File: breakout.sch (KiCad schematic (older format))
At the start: 32 parts, among them CON1 SD_Card, CON2 USB-MICRO-AB, P2 CONN_01X40, P3 CONN_01X40, P4 CONN_01X40, P5 A-DF-09-A/KG-T4S, SW1 SW_PUSH

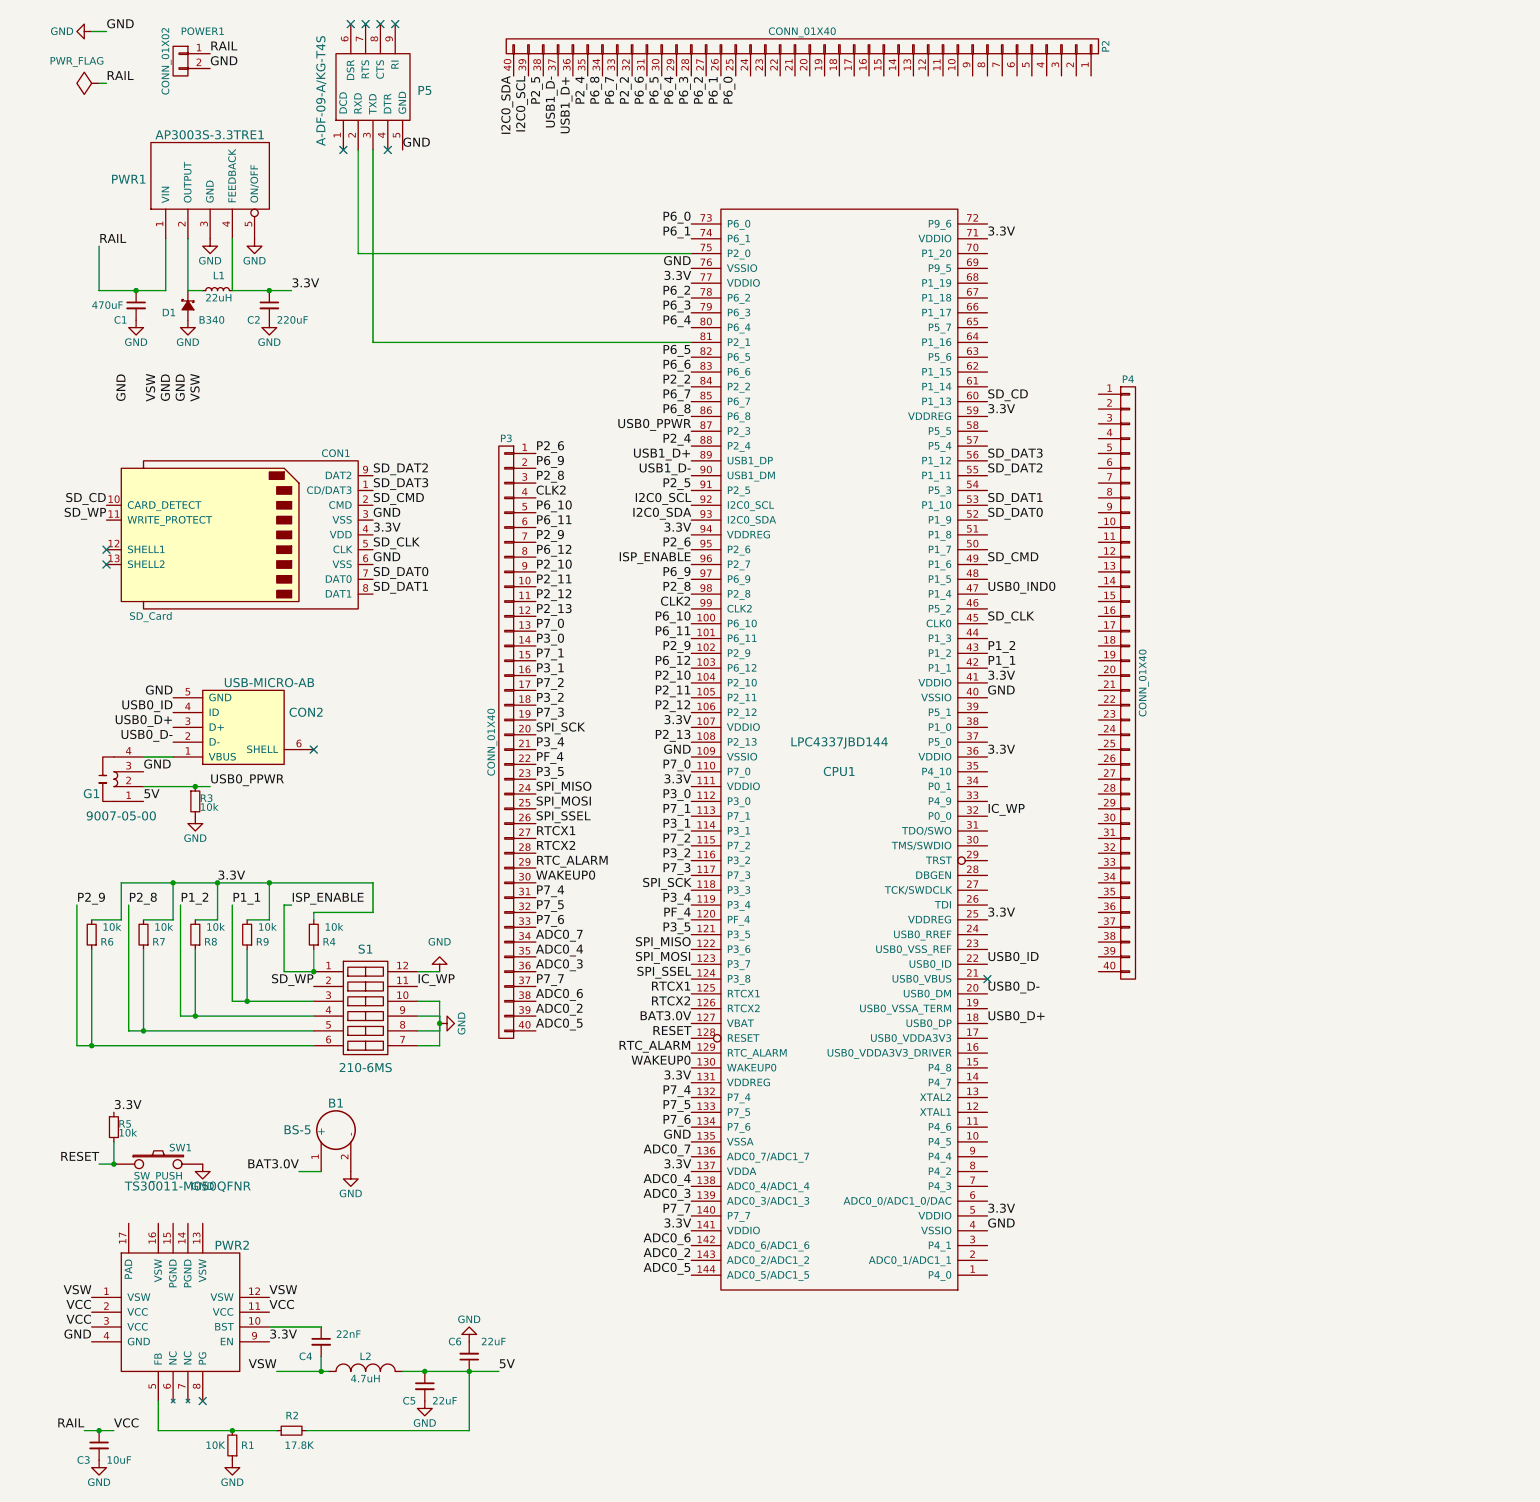
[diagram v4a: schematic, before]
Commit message: fully netlisted CPU1
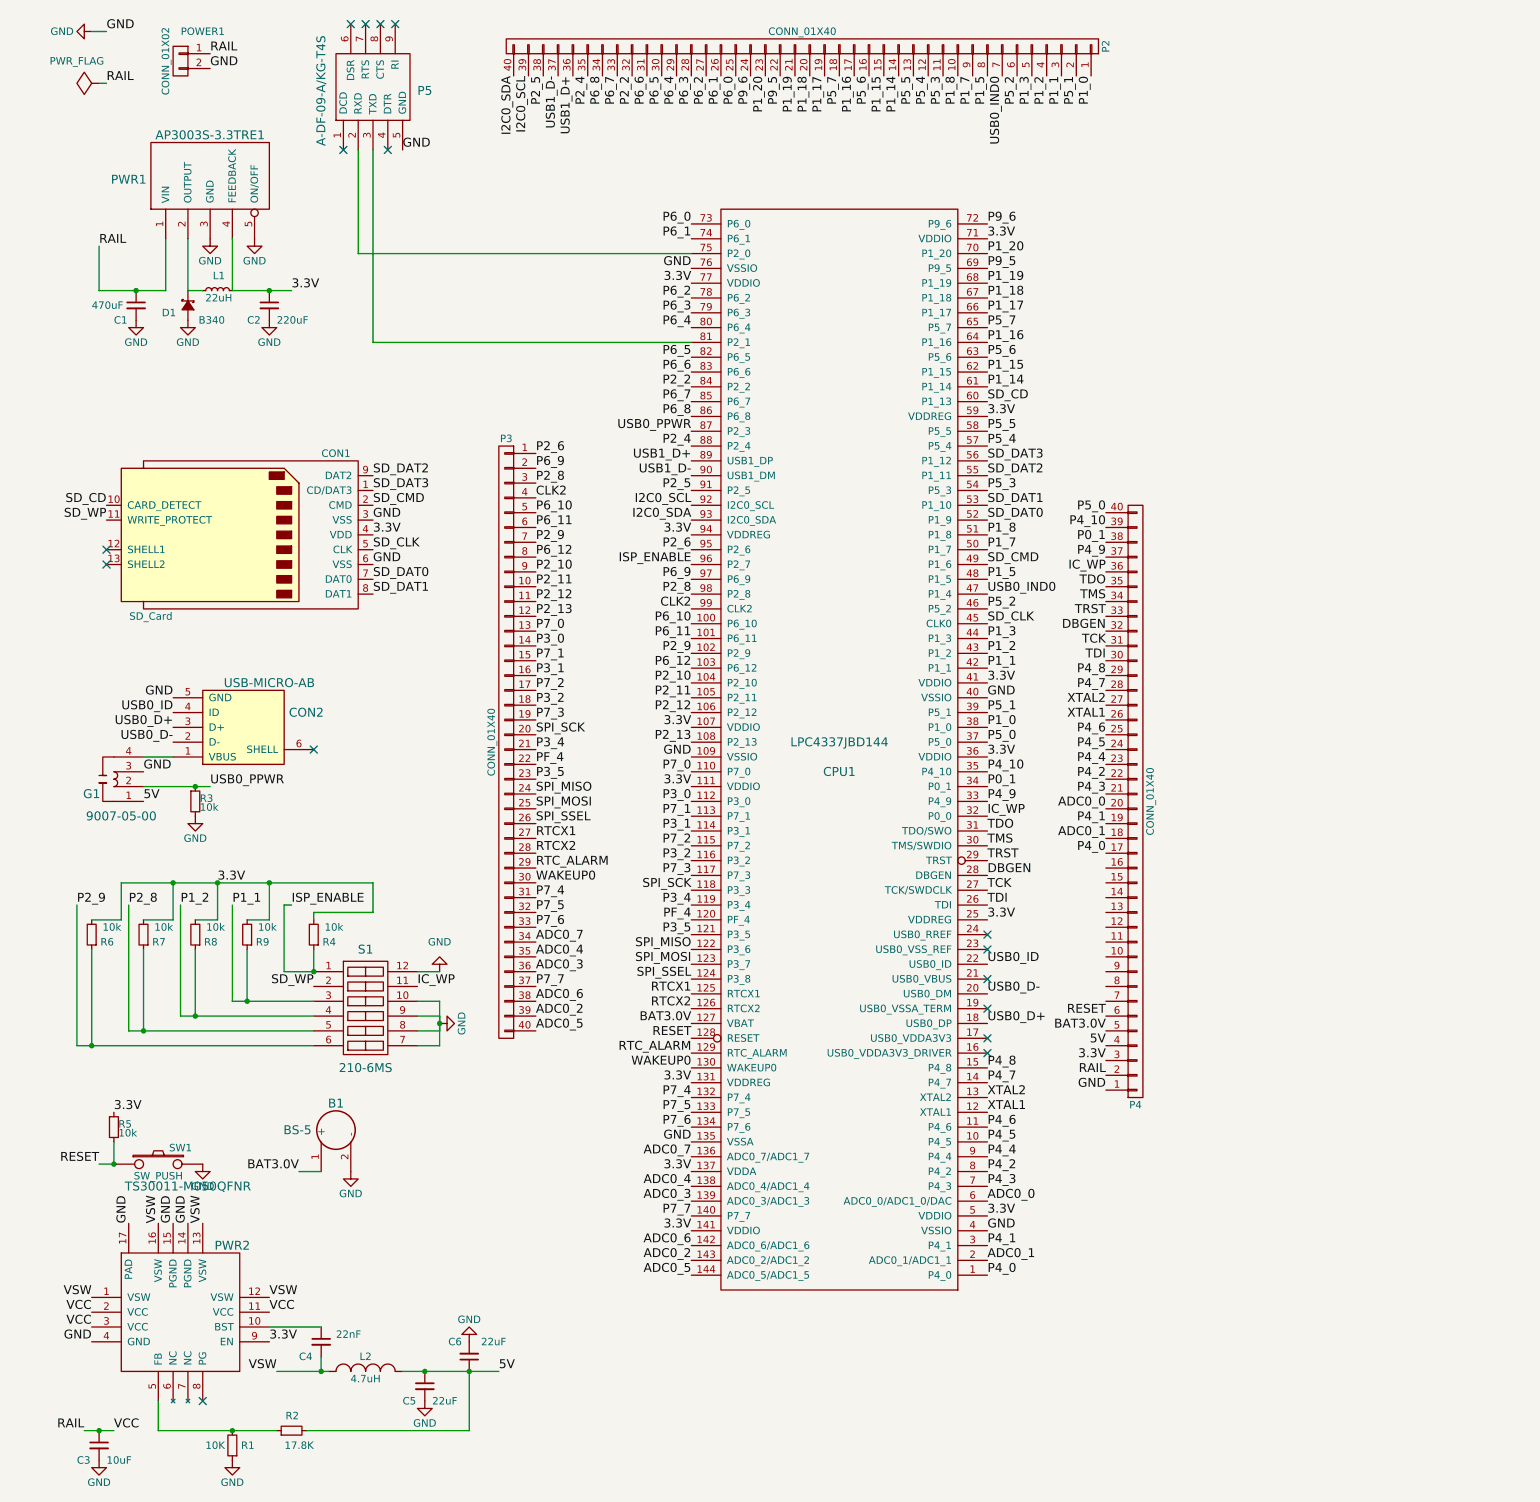
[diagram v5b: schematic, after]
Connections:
- net 3.3V: now also P4.3 (P3)
- net 5V: now also P4.4 (P4)
- net BAT3.0V: now also P4.5 (P5)
- net GND: now also P4.1 (P1), PWR2.14 (PGND), PWR2.15 (PGND), PWR2.17 (PAD)
- net IC_WP: now also P4.36 (P36)
- net P1_1: now also P2.3 (P3)
- net P1_2: now also P2.4 (P4)
- net RAIL: now also P4.2 (P2)
- net RESET: now also P4.6 (P6)
- net USB0_IND0: now also P2.7 (P7)
- net VSW: now also PWR2.13 (VSW), PWR2.16 (VSW)
- net P4_0: now reaches CPU1.1 (P4_0)
- net P4_0: now also P4.17 (P17)
- net P4_5: now reaches CPU1.10 (P4_5)
- net P4_5: now also P4.24 (P24)
- net P4_6: now reaches CPU1.11 (P4_6)
- net P4_6: now also P4.25 (P25)
- net XTAL1: now reaches CPU1.12 (XTAL1)
- net XTAL1: now also P4.26 (P26)
- net XTAL2: now reaches CPU1.13 (XTAL2)
- net XTAL2: now also P4.27 (P27)
- net P4_7: now reaches CPU1.14 (P4_7)
- net P4_7: now also P4.28 (P28)
- net P4_8: now reaches CPU1.15 (P4_8)
- net P4_8: now also P4.29 (P29)
- net ADC0_1: now reaches CPU1.2 (ADC0_1/ADC1_1)
- net ADC0_1: now also P4.18 (P18)
- net TDI: now reaches CPU1.26 (TDI)
- net TDI: now also P4.30 (P30)
- net TCK: now reaches CPU1.27 (TCK/SWDCLK)
- net TCK: now also P4.31 (P31)
- net DBGEN: now reaches CPU1.28 (DBGEN)
- net DBGEN: now also P4.32 (P32)
- net TRST: now reaches CPU1.29 (TRST)
- net TRST: now also P4.33 (P33)
- net P4_1: now reaches CPU1.3 (P4_1)
- net P4_1: now also P4.19 (P19)
- net TMS: now reaches CPU1.30 (TMS/SWDIO)
- net TMS: now also P4.34 (P34)
- net TDO: now reaches CPU1.31 (TDO/SWO)
- net TDO: now also P4.35 (P35)
- net P4_9: now reaches CPU1.33 (P4_9)
- net P4_9: now also P4.37 (P37)
- net P0_1: now reaches CPU1.34 (P0_1)
- net P0_1: now also P4.38 (P38)
- net P4_10: now reaches CPU1.35 (P4_10)
- net P4_10: now also P4.39 (P39)
- net P5_0: now reaches CPU1.37 (P5_0)
- net P5_0: now also P4.40 (P40)
- net P1_0: now reaches CPU1.38 (P1_0)
- net P1_0: now also P2.1 (P1)
- net P5_1: now reaches CPU1.39 (P5_1)
- net P5_1: now also P2.2 (P2)
- net P1_3: now reaches CPU1.44 (P1_3)
- net P1_3: now also P2.5 (P5)
- net P5_2: now reaches CPU1.46 (P5_2)
- net P5_2: now also P2.6 (P6)
- net P1_5: now reaches CPU1.48 (P1_5)
- net P1_5: now also P2.8 (P8)
- net P1_7: now reaches CPU1.50 (P1_7)
- net P1_7: now also P2.9 (P9)
- net P1_8: now reaches CPU1.51 (P1_8)
- net P1_8: now also P2.10 (P10)
- net P5_3: now reaches CPU1.54 (P5_3)
- net P5_3: now also P2.11 (P11)
- net P5_4: now reaches CPU1.57 (P5_4)
- net P5_4: now also P2.12 (P12)
- net P5_5: now reaches CPU1.58 (P5_5)
- net P5_5: now also P2.13 (P13)
- net ADC0_0: now reaches CPU1.6 (ADC0_0/ADC1_0/DAC)
- net ADC0_0: now also P4.20 (P20)
- net P1_14: now reaches CPU1.61 (P1_14)
- net P1_14: now also P2.14 (P14)
- net P1_15: now reaches CPU1.62 (P1_15)
- net P1_15: now also P2.15 (P15)
- net P5_6: now reaches CPU1.63 (P5_6)
- net P5_6: now also P2.16 (P16)
- net P1_16: now reaches CPU1.64 (P1_16)
- net P1_16: now also P2.17 (P17)
- net P5_7: now reaches CPU1.65 (P5_7)
- net P5_7: now also P2.18 (P18)
- net P1_17: now reaches CPU1.66 (P1_17)
- net P1_17: now also P2.19 (P19)
- net P1_18: now reaches CPU1.67 (P1_18)
- net P1_18: now also P2.20 (P20)
- net P1_19: now reaches CPU1.68 (P1_19)
- net P1_19: now also P2.21 (P21)
- net P9_5: now reaches CPU1.69 (P9_5)
- net P9_5: now also P2.22 (P22)
- net P4_3: now reaches CPU1.7 (P4_3)
- net P4_3: now also P4.21 (P21)
- net P1_20: now reaches CPU1.70 (P1_20)
- net P1_20: now also P2.23 (P23)
- net P9_6: now reaches CPU1.72 (P9_6)
- net P9_6: now also P2.24 (P24)
- net P4_2: now reaches CPU1.8 (P4_2)
- net P4_2: now also P4.22 (P22)
- net P4_4: now reaches CPU1.9 (P4_4)
- net P4_4: now also P4.23 (P23)
- no-connect marks 11 -> 16
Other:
- moved on the sheet: P4
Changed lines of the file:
@@
 L CONN_01X40 P4
 U 1 1 5614BB33
-P 7800 5000
-F 0 "P4" H 7800 7050 50  0000 C CNN
-F 1 "CONN_01X40" V 7900 5000 50  0000 C CNN
-F 2 "Socket_Strips:Socket_Strip_Straight_1x40" H 7800 5000 60  0001 C CNN
-F 3 "" H 7800 5000 60  0000 C CNN
-	1    7800 5000
-	1    0    0    -1
+P 7850 5800
+F 0 "P4" H 7850 7850 50  0000 C CNN
+F 1 "CONN_01X40" V 7950 5800 50  0000 C CNN
+F 2 "Socket_Strips:Socket_Strip_Straight_1x40" H 7850 5800 60  0001 C CNN
+F 3 "" H 7850 5800 60  0000 C CNN
+	1    7850 5800
+	1    0    0    1
 $EndComp
 $Comp
@@
 Text Label 2000 9450 0    60   ~ 0
 3.3V
-Text Label 1050 3100 1    60   ~ 0
+Text Label 1050 8650 1    60   ~ 0
 GND
 Text Label 800  9450 2    60   ~ 0
 GND
-Text Label 1350 3100 1    60   ~ 0
-GND
-Text Label 1450 3100 1    60   ~ 0
-GND
-Text Label 1250 3100 1    60   ~ 0
+Text Label 1350 8650 1    60   ~ 0
+GND
+Text Label 1450 8650 1    60   ~ 0
+GND
+Text Label 1250 8650 1    60   ~ 0
 VSW
-Text Label 1550 3100 1    60   ~ 0
+Text Label 1550 8650 1    60   ~ 0
 VSW
 Text Label 2000 9150 0    60   ~ 0
@@
 	1850 6600 2000 6600
 Wire Wire Line
-	2000 6600 2000 6350
+	2000 6350 2000 6600
 Wire Wire Line
 	1000 6350 2700 6350
@@
 Text Label 5150 900  3    60   ~ 0
 P6_0
+Text Label 6850 9000 0    60   ~ 0
+P4_0
+Text Label 6850 8900 0    60   ~ 0
+ADC0_1
+Text Label 6850 8800 0    60   ~ 0
+P4_1
+Text Label 6850 8500 0    60   ~ 0
+ADC0_0
+Text Label 6850 8400 0    60   ~ 0
+P4_3
+Text Label 6850 8300 0    60   ~ 0
+P4_2
+Text Label 6850 8200 0    60   ~ 0
+P4_4
+Text Label 6850 8100 0    60   ~ 0
+P4_5
+Text Label 6850 8000 0    60   ~ 0
+P4_6
+Text Label 6850 7900 0    60   ~ 0
+XTAL1
+Text Label 6850 7800 0    60   ~ 0
+XTAL2
+Text Label 6850 7700 0    60   ~ 0
+P4_7
+Text Label 6850 7600 0    60   ~ 0
+P4_8
+NoConn ~ 6850 7500
+NoConn ~ 6850 7400
+NoConn ~ 6850 7200
+NoConn ~ 6850 6800
+NoConn ~ 6850 6700
+Text Label 6850 6400 0    60   ~ 0
+TCK
+Text Label 6850 6300 0    60   ~ 0
+DBGEN
+Text Label 6850 6200 0    60   ~ 0
+TRST
+Text Label 6850 6100 0    60   ~ 0
+TMS
+Text Label 6850 6000 0    60   ~ 0
+TDO
+Text Label 6850 5800 0    60   ~ 0
+P4_9
+Text Label 6850 5700 0    60   ~ 0
+P0_1
+Text Label 6850 5600 0    60   ~ 0
+P4_10
+Text Label 6850 5400 0    60   ~ 0
+P5_0
+Text Label 6850 5300 0    60   ~ 0
+P1_0
+Text Label 6850 5200 0    60   ~ 0
+P5_1
+Text Label 6850 4700 0    60   ~ 0
+P1_3
+Text Label 6850 4500 0    60   ~ 0
+P5_2
+Text Label 6850 4300 0    60   ~ 0
+P1_5
+Text Label 6850 4100 0    60   ~ 0
+P1_7
+Text Label 6850 4000 0    60   ~ 0
+P1_8
+Text Label 6850 3700 0    60   ~ 0
+P5_3
+Text Label 6850 3400 0    60   ~ 0
+P5_4
+Text Label 6850 3300 0    60   ~ 0
+P5_5
+Text Label 6850 3000 0    60   ~ 0
+P1_14
+Text Label 6850 2900 0    60   ~ 0
+P1_15
+Text Label 6850 2800 0    60   ~ 0
+P5_6
+Text Label 6850 2700 0    60   ~ 0
+P1_16
+Text Label 6850 2600 0    60   ~ 0
+P5_7
+Text Label 6850 2500 0    60   ~ 0
+P1_17
+Text Label 6850 2400 0    60   ~ 0
+P1_18
+Text Label 6850 2300 0    60   ~ 0
+P1_19
+Text Label 6850 2200 0    60   ~ 0
+P9_5
+Text Label 6850 2100 0    60   ~ 0
+P1_20
+Text Label 6850 1900 0    60   ~ 0
+P9_6
+Text Label 6850 6500 0    60   ~ 0
+TDI
+Text Label 7350 900  3    60   ~ 0
+P1_1
+Text Label 7250 900  3    60   ~ 0
+P1_2
+Text Label 7150 900  3    60   ~ 0
+P1_3
+Text Label 7050 900  3    60   ~ 0
+P5_2
+Text Label 6850 900  3    60   ~ 0
+P1_5
+Text Label 6750 900  3    60   ~ 0
+P1_7
+Text Label 6650 900  3    60   ~ 0
+P1_8
+Text Label 6550 900  3    60   ~ 0
+P5_3
+Text Label 6450 900  3    60   ~ 0
+P5_4
+Text Label 6350 900  3    60   ~ 0
+P5_5
+Text Label 6250 900  3    60   ~ 0
+P1_14
+Text Label 6150 900  3    60   ~ 0
+P1_15
+Text Label 6050 900  3    60   ~ 0
+P5_6
+Text Label 5950 900  3    60   ~ 0
+P1_16
+Text Label 5850 900  3    60   ~ 0
+P5_7
+Text Label 5750 900  3    60   ~ 0
+P1_17
+Text Label 5650 900  3    60   ~ 0
+P1_18
+Text Label 5550 900  3    60   ~ 0
+P1_19
+Text Label 5450 900  3    60   ~ 0
+P9_5
+Text Label 5350 900  3    60   ~ 0
+P1_20
+Text Label 5250 900  3    60   ~ 0
+P9_6
+Text Label 6950 900  3    60   ~ 0
+USB0_IND0
+Text Label 7550 900  3    60   ~ 0
+P1_0
+Text Label 7450 900  3    60   ~ 0
+P5_1
+Text Label 7650 4250 2    60   ~ 0
+IC_WP
+Text Label 7650 6150 2    60   ~ 0
+P4_0
+Text Label 7650 6050 2    60   ~ 0
+ADC0_1
+Text Label 7650 5950 2    60   ~ 0
+P4_1
+Text Label 7650 5850 2    60   ~ 0
+ADC0_0
+Text Label 7650 5750 2    60   ~ 0
+P4_3
+Text Label 7650 5650 2    60   ~ 0
+P4_2
+Text Label 7650 5550 2    60   ~ 0
+P4_4
+Text Label 7650 5450 2    60   ~ 0
+P4_5
+Text Label 7650 5350 2    60   ~ 0
+P4_6
+Text Label 7650 5250 2    60   ~ 0
+XTAL1
+Text Label 7650 5150 2    60   ~ 0
+XTAL2
+Text Label 7650 5050 2    60   ~ 0
+P4_7
+Text Label 7650 4950 2    60   ~ 0
+P4_8
+Text Label 7650 4750 2    60   ~ 0
+TCK
+Text Label 7650 4650 2    60   ~ 0
+DBGEN
+Text Label 7650 4550 2    60   ~ 0
+TRST
+Text Label 7650 4450 2    60   ~ 0
+TMS
+Text Label 7650 4350 2    60   ~ 0
+TDO
+Text Label 7650 4150 2    60   ~ 0
+P4_9
+Text Label 7650 4050 2    60   ~ 0
+P0_1
+Text Label 7650 3950 2    60   ~ 0
+P4_10
+Text Label 7650 3850 2    60   ~ 0
+P5_0
+Text Label 7650 4850 2    60   ~ 0
+TDI
+Text Label 7650 7650 2    60   ~ 0
+RAIL
+Text Label 7650 7750 2    60   ~ 0
+GND
+Text Label 7650 7550 2    60   ~ 0
+3.3V
+Text Label 7650 7450 2    60   ~ 0
+5V
+Text Label 7650 7350 2    60   ~ 0
+BAT3.0V
+Text Label 7650 7250 2    60   ~ 0
+RESET
 $EndSCHEMATC
